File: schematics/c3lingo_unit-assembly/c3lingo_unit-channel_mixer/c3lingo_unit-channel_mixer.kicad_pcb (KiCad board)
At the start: 2 copper layers, 75 x 90 mm, 87 parts, among them J301 Interconnect, J302 PowerSupply, J303 I/O, SW301 OnAir_X, SW302 Mute_X, U301 LM833-N, U302 LM339, U303 LM339, U304 LM339, U305 LM833-N

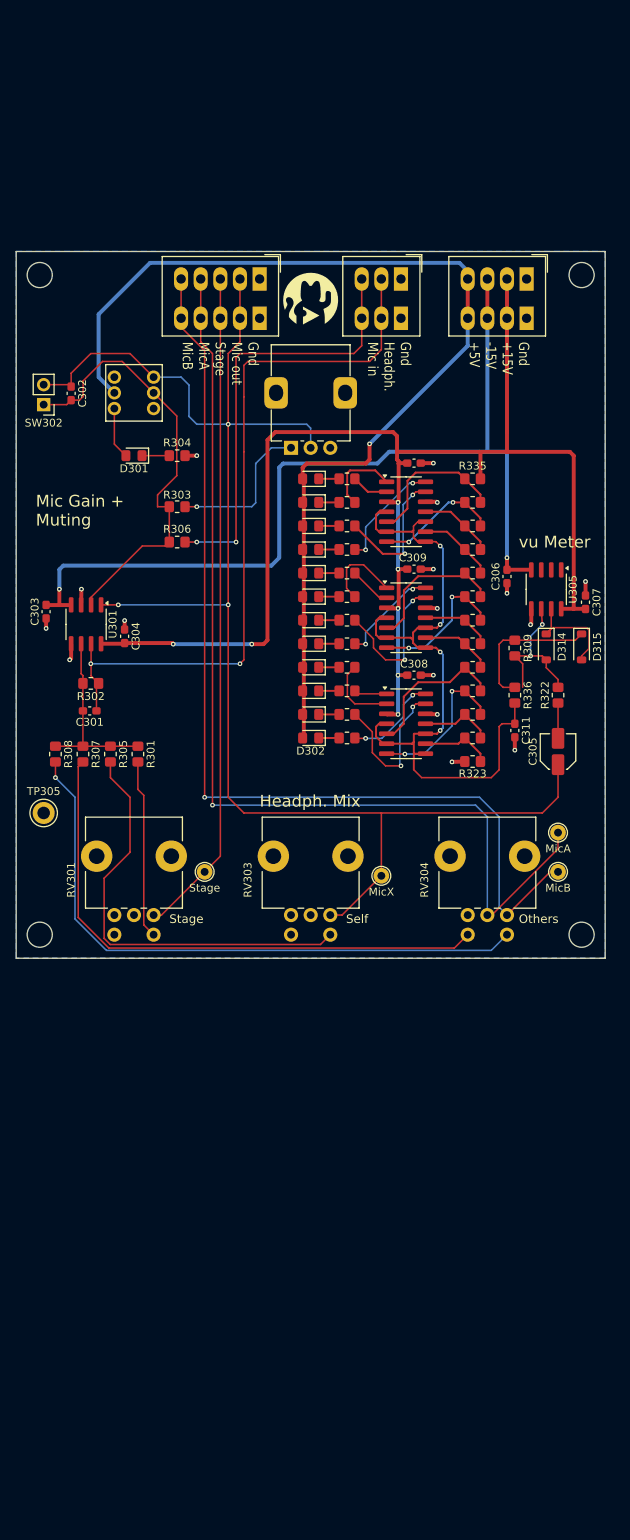
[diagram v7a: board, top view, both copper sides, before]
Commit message: Channel Mixer: Rework muting mechanism
Note: Schematic PDF not updated yet
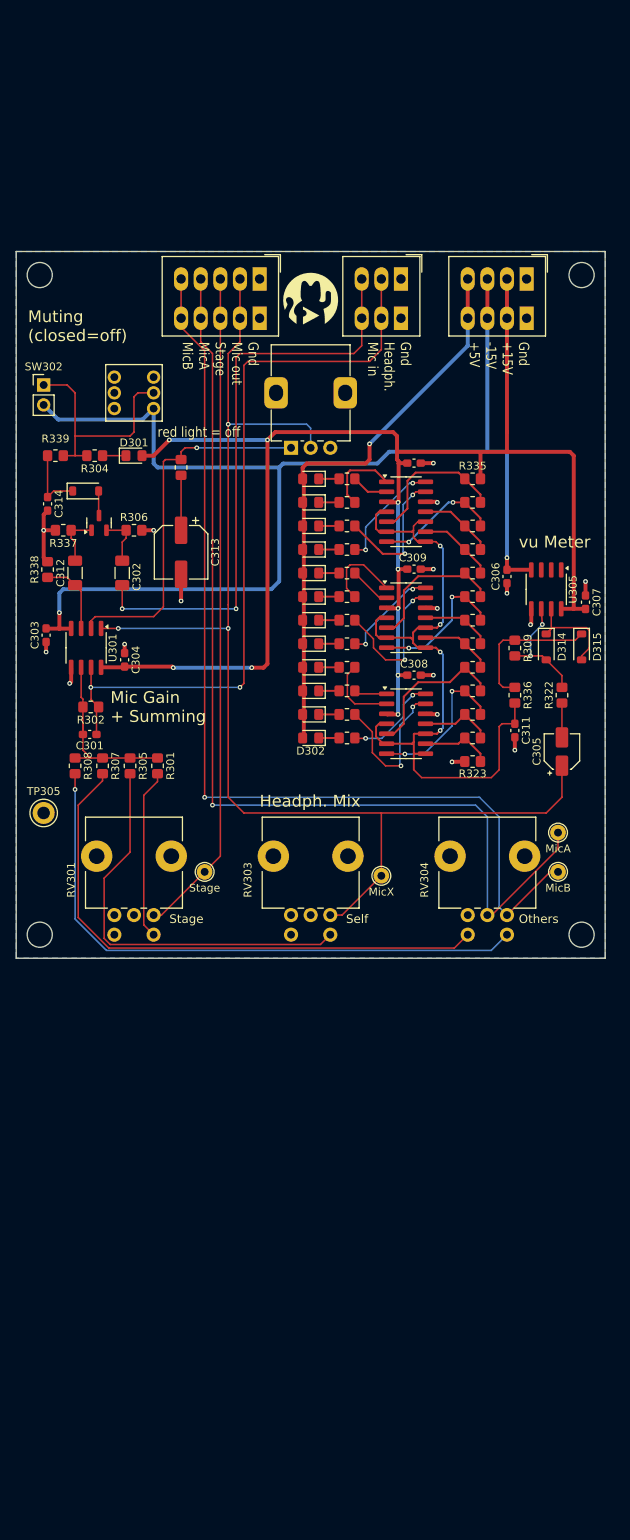
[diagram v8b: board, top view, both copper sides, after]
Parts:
- added C312: 100nF C0G, Capacitor_SMD:C_1206_3216Metric_Pad1.33x1.80mm_HandSolder, F.Cu at (57.5, 120.9)
- added C313: 47uF, Capacitor_SMD:CP_Elec_6.3x5.4, F.Cu at (71.0, 118.3)
- added C314: 1uF, Capacitor_SMD:C_0603_1608Metric_Pad1.08x0.95mm_HandSolder, F.Cu at (54.0, 112.1)
- added D316: 1N4148, Diode_SMD:D_SOD-123, F.Cu at (58.9, 110.5)
- added Q301: MMBFJ113, Package_TO_SOT_SMD:SOT-23, F.Cu at (60.5, 114.6)
- added R337: 1M, Resistor_SMD:R_0805_2012Metric_Pad1.20x1.40mm_HandSolder, F.Cu at (56.0, 115.5)
- added R338: 1M, Resistor_SMD:R_0805_2012Metric_Pad1.20x1.40mm_HandSolder, F.Cu at (54.0, 120.5)
- added R339: 1M, Resistor_SMD:R_0805_2012Metric_Pad1.20x1.40mm_HandSolder, F.Cu at (55.0, 106.0)
- C302: value 1nF -> 100nF C0G; footprint Capacitor_SMD:C_0603_1608Metric_Pad1.08x0.95mm_HandSolder -> Capacitor_SMD:C_1206_3216Metric_Pad1.33x1.80mm_HandSolder
- C305: footprint Capacitor_SMD:C_Elec_4x5.8 -> Capacitor_SMD:CP_Elec_4x5.8
- D301: value On-Air (rd) -> muted (rd)
- R303: value 56R -> 68R (TODO 330R for 50K)
- R304: value 150R -> 10k
- R306: value 330R -> 1M
- RV302: value 10K log. -> 10K log. (TODO 50K)
- U301: value LM833-N -> TL072
- moved C302 23.8 mm to (63.5, 120.9)
- moved R304 10.5 mm to (60.0, 106.0), turned to 180 degrees
- moved R306 5.70 mm to (65.0, 115.5)
- moved R303 5.02 mm to (71.0, 107.5), turned to -90 degrees
- moved C303 3.00 mm to (53.8, 128.9)
- moved C301 3.00 mm to (59.4, 141.5)
- moved C304 3.00 mm to (63.8, 132.0)
- moved R302 3.00 mm to (59.5, 138.0)
- moved U301 3.00 mm to (58.9, 130.5)
- moved R301 2.92 mm to (68.0, 145.5)
- moved R305 2.92 mm to (64.5, 145.5)
- moved R307 2.92 mm to (61.0, 145.5)
- moved R308 2.92 mm to (57.5, 145.5)
- moved SW302 2.50 mm to (53.5, 97.0), turned to 0 degrees
- moved C305 0.50 mm to (119.5, 143.7)
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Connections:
- C302 pad 1: /Mic_X -> Net-(Q301-S)
- C302 pad 2: Net-(SW301A-B) -> /MicPre
- D301 pad 2: Net-(D301-A) -> +15V
- R303 pad 1: Net-(R303-Pad1) -> Net-(U301A--)
- R303 pad 2: Net-(SW301A-B) -> Net-(C313-Pad1)
- R304 pad 2: GND -> Net-(SW301A-B)
- R306 pad 1: Net-(SW301A-B) -> Net-(Q301-S)
- R306 pad 2: /MicPre -> GND
- RV302 pad 1: Net-(R303-Pad1) -> Net-(U301A--)
- SW301 pad 1: /Mic_X -> unconnected-(SW301A-A-Pad1)
- SW301 pad 3: unconnected-(SW301A-C-Pad3) -> -15V
- SW301 pad 4: unconnected-(SW301B-A-Pad4) -> (no net)
- SW301 pad 5: +5V -> (no net)
- SW301 pad 6: Net-(D301-A) -> (no net)
- SW302 pad 2: /Mic_X -> -15V
- U301 pad 2: Net-(SW301A-B) -> Net-(U301A--)
- U301 pad 3: GND -> Net-(U301A-+)
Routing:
- net +5V: track 133.5 -> 72.6 mm
- net Net-(U301A--): track 0.00 -> 48.1 mm, vias 0 -> 1
- net -15V: track 117.7 -> 159.3 mm
- net /Mic_X: track 192.5 -> 161.1 mm
- net Net-(SW301A-B): track 55.7 -> 30.3 mm
- net Net-(R303-Pad1): track 20.6 -> 0.00 mm, vias 1 -> 0
- net +15V: track 178.4 -> 198.2 mm, vias 7 -> 9
- net /MicPre: track 55.1 -> 74.6 mm
- net GND: track 25.6 -> 35.3 mm, vias 16 -> 17
- net Net-(U301A-+): track 0.00 -> 9.73 mm
- net Net-(D316-K): track 0.00 -> 8.80 mm
- net Net-(Q301-D): track 0.00 -> 7.08 mm
- net Net-(C313-Pad1): track 0.00 -> 7.00 mm
- net Net-(Q301-S): track 0.00 -> 6.68 mm
- net Net-(D301-A): track 6.61 -> 0.00 mm
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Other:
- board text added: "Mic Gain + Summing"
- board text added: "Muting (closed=off)"
- board text added: "c3lingo Interpreter Unit Channel Mixer v0.3.1 2024-08-30"
- board text added: "red light = off"
- board text removed: "Mic Gain + Muting"
- board text removed: "c3lingo Interpreter Unit Channel Mixer v0.3.1 2024-07-08"
